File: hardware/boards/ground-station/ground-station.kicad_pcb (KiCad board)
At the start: 4 copper layers, 65 x 56.5 mm, 118 parts, among them J1 USB_A, J101 Raspberry_Pi_2_3, J102 Conn_01x15, J2 Barrel_Jack, J201 U.FL, J202 U.FL, J203 U.FL, J3 Conn_Coaxial, U201 SX1262IMLTRT, U202 RX5808, U203 SW-GPS01, U204 SKY13453-385LF, U3 TPS564242DRLR, U601 ADV7282A-M, U602 AP2127K-1.8, U603 AP2127K-1.8, Y201 32 MHz, Y601 28.63636 MHz

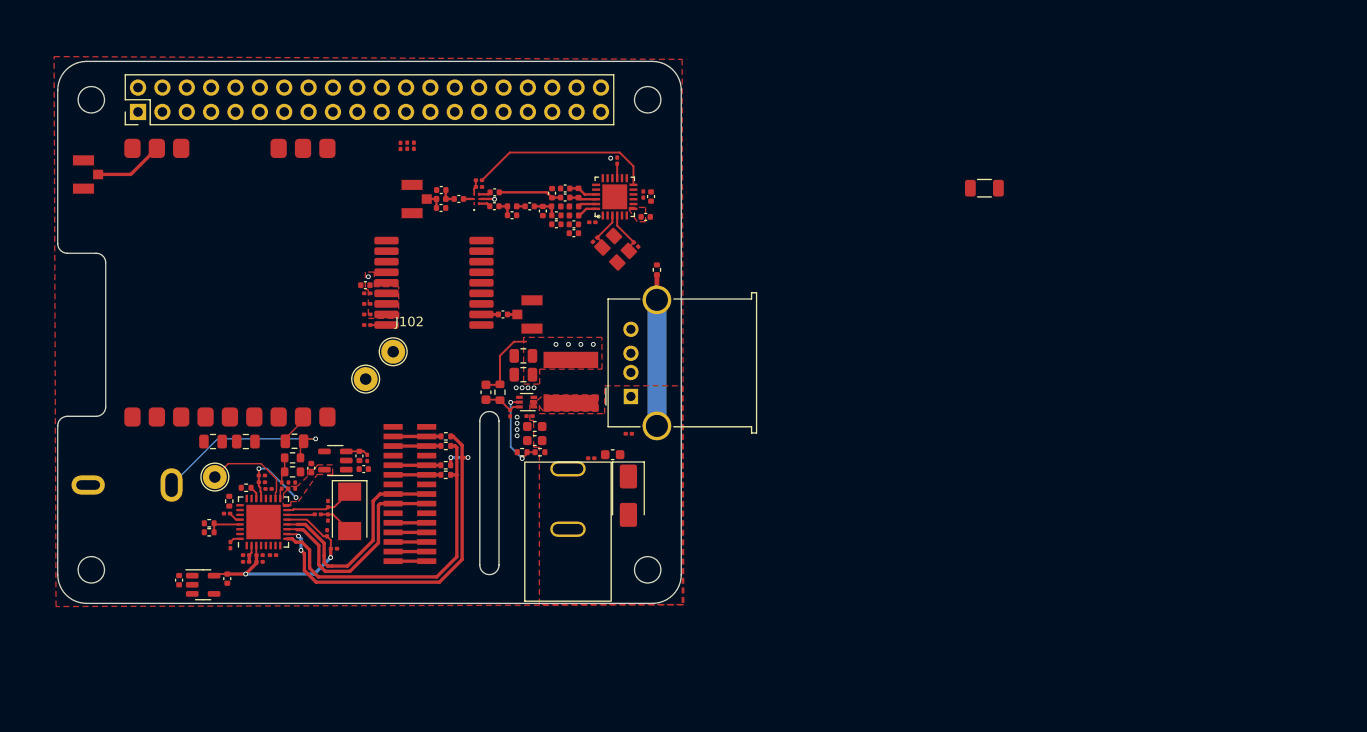
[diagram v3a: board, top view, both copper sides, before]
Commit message: Finished initial layout
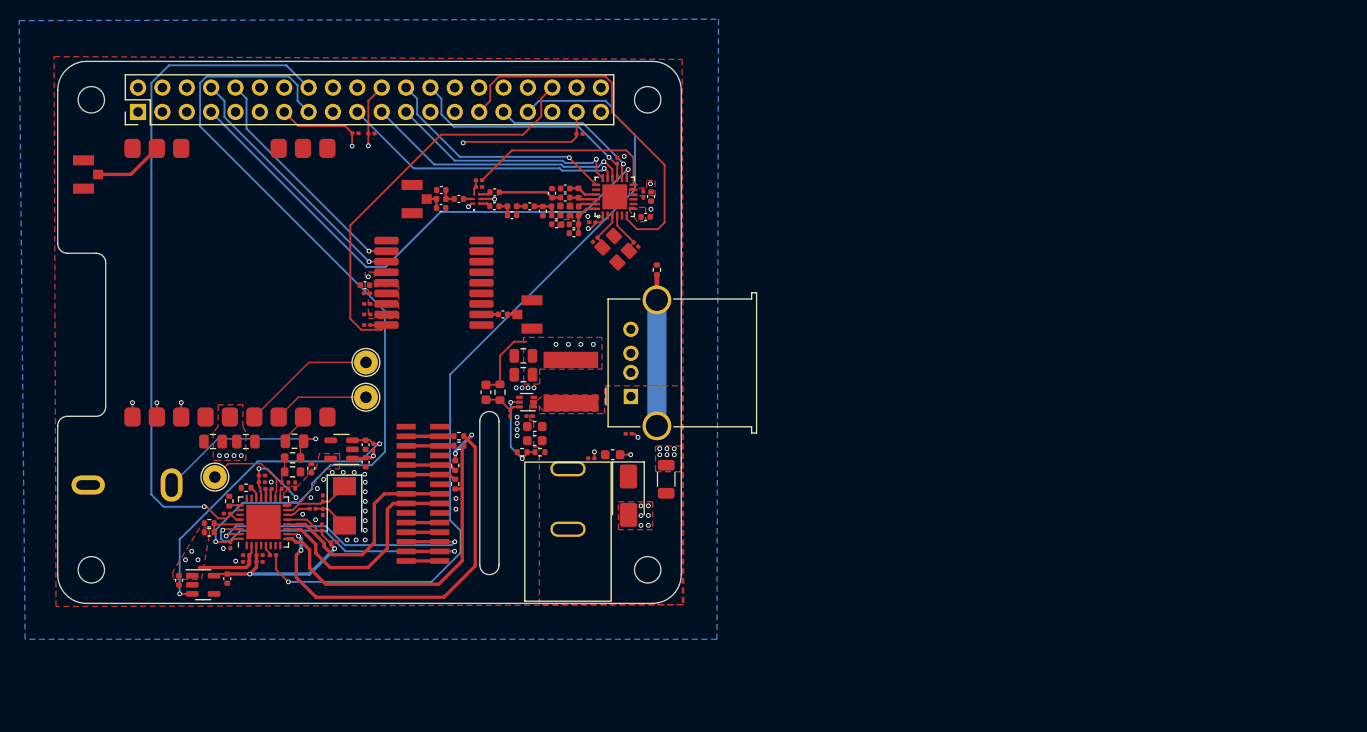
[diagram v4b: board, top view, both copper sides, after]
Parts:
- moved R3 45.0 mm to (163.6, 109.4), turned to 90 degrees
- moved R203 18.0 mm to (154.6, 73.4), turned to 0 degrees
- moved R204 4.88 mm to (131.2, 73.4), turned to 0 degrees
- moved R202 4.61 mm to (132.9, 73.4), turned to 0 degrees
- moved TP1 3.05 mm to (132.3, 97.3)
- moved TP2 1.89 mm to (132.3, 100.9)
- moved R24 1.37 mm to (141.6, 109.9), turned to 90 degrees
- moved J102 1.36 mm to (138.3, 111.0)
- moved R25 1.36 mm to (142.0, 105.0)
- moved R26 1.36 mm to (142.0, 106.0)
- moved C610 1.33 mm to (132.3, 105.8)
- moved R606 1.33 mm to (133.1, 106.1)
- moved U603 1.33 mm to (129.8, 106.3)
- moved R23 0.98 mm to (141.6, 108.0), turned to -90 degrees
- moved C603 0.79 mm to (127.8, 112.8)
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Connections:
- J201 pad 2: unconnected-(J201-Ext-Pad2) -> GND
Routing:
- net /~{DIGITIZER_INTRQ}: track 0.00 -> 87.9 mm, vias 0 -> 1
- net /~{DIGITIZER_PWRDWN}: track 1.14 -> 85.8 mm, vias 0 -> 1
- net /~{DIGITIZER_RESET}: track 1.30 -> 71.9 mm, vias 0 -> 1
- net /VIDEO_CH2: track 0.00 -> 60.4 mm, vias 0 -> 2
- net /DIGITAL_RADIO_DIO1: track 0.00 -> 55.3 mm, vias 0 -> 1
- net +5V: track 0.00 -> 52.8 mm, vias 0 -> 4
- net /VIDEO_CH1: track 0.00 -> 49.4 mm, vias 0 -> 2
- net /VIDEO_CH3: track 0.00 -> 45.0 mm, vias 0 -> 2
- net /~{GPS_RESET}: track 1.68 -> 44.0 mm
- net /DIGITAL_RADIO_DIO3: track 0.00 -> 38.5 mm
- net /Video Digitizer/VID_EN_1V8: track 2.34 -> 35.0 mm, vias 0 -> 2
- net /CAM_SDA: track 3.50 -> 33.7 mm, vias 0 -> 2
- net /DIGITAL_RADIO_MOSI: track 0.00 -> 29.5 mm, vias 0 -> 1
- net /CAM_SCL: track 3.50 -> 31.8 mm, vias 0 -> 2
- net /DIGITAL_RADIO_MISO: track 0.00 -> 27.9 mm, vias 0 -> 1
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- added copper zone on In2.Cu, net +3V3
- added copper zone on In2.Cu, net +5V
- added copper zone on B.Cu, net GND
- added copper zone on F.Cu, net Net-(C219-Pad1)
- added copper zone on F.Cu, net Net-(J101-5V-Pad2)
- added copper zone on In2.Cu, net Net-(J101-5V-Pad2)

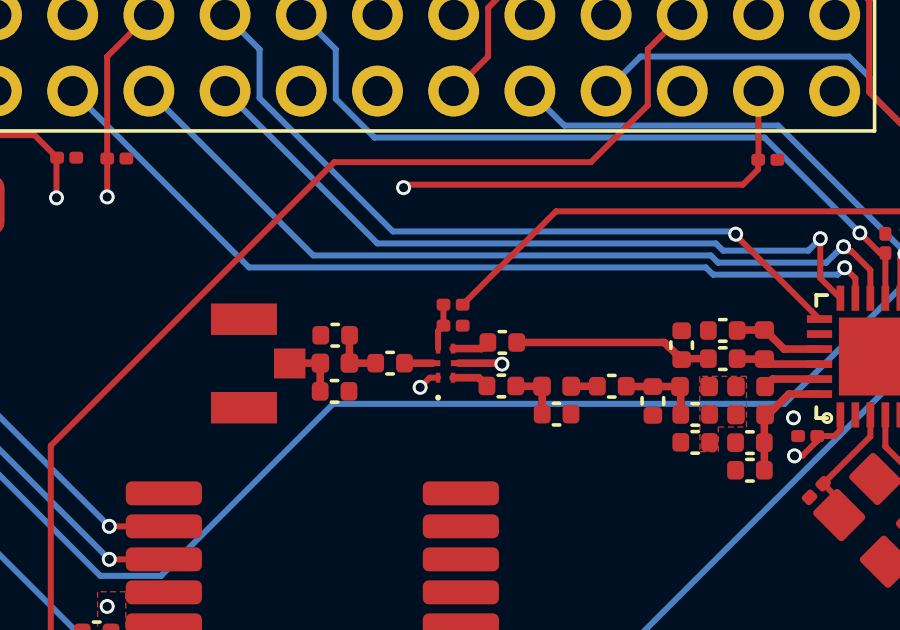
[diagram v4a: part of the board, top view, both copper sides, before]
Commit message: Added voltage divider to RF switch VTCL pin to keep voltage to 1.8V. Adjusted cap size to keep RC cutoff frequency consistent
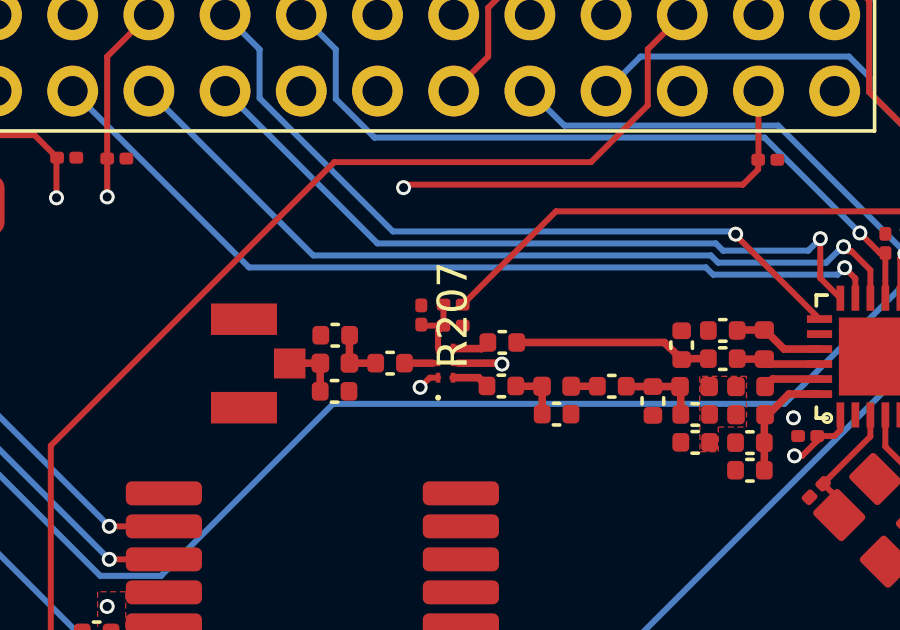
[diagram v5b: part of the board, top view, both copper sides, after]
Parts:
- added R207: 2.7k, Resistor_SMD:R_0201_0603Metric, F.Cu at (143.0, 78.6)
- C226: value 1n -> 100p
- R206: value 100R -> 2.2k
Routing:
- net Net-(U204-VTCL): track 1.54 -> 2.29 mm
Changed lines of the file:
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@@
         (effects (font (size 1 1) (thickness 0.15)))
     )
-    (fp_text value "1n" (at 0 1.05) (layer "F.Fab")
+    (fp_text value "100p" (at 0 1.05) (layer "F.Fab")
         (effects (font (size 1 1) (thickness 0.15)))
     )
@@
         (effects (font (size 1 1) (thickness 0.15)))
     )
-    (fp_text value "100R" (at 0 1.05) (layer "F.Fab")
+    (fp_text value "2.2k" (at 0 1.05) (layer "F.Fab")
         (effects (font (size 1 1) (thickness 0.15)))
     )
@@
   )
   (footprint "Resistor_SMD:R_0201_0603Metric" (layer "F.Cu")
+    (at 143.04 78.615 -90)
+    (descr "Resistor SMD 0201 (0603 Metric), square (rectangular) end terminal, IPC_7351 nominal, (Body size source: https://www.vishay.com/docs/20052/crcw0201e3.pdf), generated with kicad-footprint-generator")
+    (tags "resistor")
+    (property "Sheetfile" "radio.kicad_sch")
+    (property "Sheetname" "Radios")
+    (property "ki_description" "Resistor")
+    (property "ki_keywords" "R res resistor")
+    (attr smd)
+    (fp_text reference "R207" (at 0 -1.05 90) (layer "F.SilkS")
+        (effects (font (size 1 1) (thickness 0.15)))
+    )
+    (fp_text value "2.7k" (at 0 1.05 90) (layer "F.Fab")
+        (effects (font (size 1 1) (thickness 0.15)))
+    )
+    (fp_text user "${REFERENCE}" (at 0 -0.68 90) (layer "F.Fab")
+        (effects (font (size 0.25 0.25) (thickness 0.04)))
+    )
+    (fp_line (start -0.7 -0.35) (end 0.7 -0.35)
+      (stroke (width 0.05) (type solid)) (layer "F.CrtYd"))
+    (fp_line (start -0.7 0.35) (end -0.7 -0.35)
+      (stroke (width 0.05) (type solid)) (layer "F.CrtYd"))
+    (fp_line (start 0.7 -0.35) (end 0.7 0.35)
+      (stroke (width 0.05) (type solid)) (layer "F.CrtYd"))
+    (fp_line (start 0.7 0.35) (end -0.7 0.35)
+      (stroke (width 0.05) (type solid)) (layer "F.CrtYd"))
+    (fp_line (start -0.3 -0.15) (end 0.3 -0.15)
+      (stroke (width 0.1) (type solid)) (layer "F.Fab"))
+    (fp_line (start -0.3 0.15) (end -0.3 -0.15)
+      (stroke (width 0.1) (type solid)) (layer "F.Fab"))
+    (fp_line (start 0.3 -0.15) (end 0.3 0.15)
+      (stroke (width 0.1) (type solid)) (layer "F.Fab"))
+    (fp_line (start 0.3 0.15) (end -0.3 0.15)
+      (stroke (width 0.1) (type solid)) (layer "F.Fab"))
+    (pad "" smd roundrect (at -0.345 0 270) (size 0.318 0.36) (layers "F.Paste") (roundrect_rratio 0.25))
+    (pad "" smd roundrect (at 0.345 0 270) (size 0.318 0.36) (layers "F.Paste") (roundrect_rratio 0.25))
+    (pad "1" smd roundrect (at -0.32 0 270) (size 0.46 0.4) (layers "F.Cu" "F.Mask") (roundrect_rratio 0.25)
+      (net 3 "GND") (pintype "passive"))
+    (pad "2" smd roundrect (at 0.32 0 270) (size 0.46 0.4) (layers "F.Cu" "F.Mask") (roundrect_rratio 0.25)
+      (net 31 "Net-(U204-VTCL)") (pintype "passive"))
+    (model "${KICAD6_3DMODEL_DIR}/Resistor_SMD.3dshapes/R_0201_0603Metric.wrl"
+      (offset (xyz 0 0 0))
+      (scale (xyz 1 1 1))
+      (rotate (xyz 0 0 0))
+    )
+  )
+  (footprint "Resistor_SMD:R_0201_0603Metric" (layer "F.Cu")
     (at 132.89 73.4)
     (descr "Resistor SMD 0201 (0603 Metric), square (rectangular) end terminal, IPC_7351 nominal, (Body size source: https://www.vishay.com/docs/20052/crcw0201e3.pdf), generated with kicad-footprint-generator")
@@
   (segment (start 145.055 79.735) (end 145.26 79.53) (width 0.254) (layer "F.Cu") (net 30))
   (segment (start 143.6 79.735) (end 143.6 79.15) (width 0.2) (layer "F.Cu") (net 31))
+  (segment (start 143.075 78.97) (end 143.04 78.935) (width 0.2) (layer "F.Cu") (net 31))
   (segment (start 143.6 79.15) (end 143.78 78.97) (width 0.2) (layer "F.Cu") (net 31))
+  (segment (start 143.78 78.97) (end 143.075 78.97) (width 0.2) (layer "F.Cu") (net 31))
   (segment (start 143.78 78.97) (end 143.78 78.27) (width 0.2) (layer "F.Cu") (net 31))
   (segment (start 140.645 79.295) (end 140.65 79.29) (width 0.254) (layer "F.Cu") (net 33))

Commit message: base station layout review
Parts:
- added C231: 100n, Capacitor_SMD:C_0201_0603Metric, F.Cu at (155.9, 82.7)
- added R208: 0, Resistor_SMD:R_0402_1005Metric, F.Cu at (127.1, 105.5)
- moved R23 14.3 mm to (140.8, 122.2), turned to 90 degrees
- moved R24 13.9 mm to (142.7, 123.8), turned to -45 degrees
- moved R25 13.3 mm to (142.1, 118.2), turned to 90 degrees
- moved C227 12.7 mm to (143.3, 81.5)
- moved R26 10.6 mm to (143.3, 116.5), turned to 90 degrees
- turned J102 to 180 degrees
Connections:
- J3 pad 1: /Radios/VIDEO_OUT -> Net-(J3-In)
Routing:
- net /CAM_CK_N: track 22.4 -> 50.0 mm
- net /CAM_CK_P: track 23.3 -> 50.1 mm
- net Net-(J3-In): track 0.00 -> 17.6 mm, vias 0 -> 1
- net /Radios/VIDEO_OUT: track 20.2 -> 3.32 mm, vias 1 -> 0
- net /CAM_D1_CONN_P: track 5.38 -> 18.6 mm, vias 0 -> 2
- net /CAM_D1_CONN_N: track 5.34 -> 15.3 mm, vias 0 -> 2
- net /CAM_SDA: track 33.7 -> 39.5 mm
- net /CAM_D0_P: track 35.4 -> 41.1 mm
- net /CAM_D0_N: track 44.9 -> 39.9 mm, vias 4 -> 0
- net unconnected-(J102-Pin_15-Pad15): track 3.50 -> 0.00 mm
- net /CAM_SCL: track 31.8 -> 35.2 mm
- net /CAM_D0_CONN_P: track 4.99 -> 7.18 mm
- net /CAM_D0_CONN_N: track 4.99 -> 6.66 mm
- net /~{DIGITIZER_INTRQ}: track 87.9 -> 86.5 mm
- net +5V: track 52.8 -> 54.0 mm
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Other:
- board size 65 x 56.5 mm -> 65 x 59.5 mm

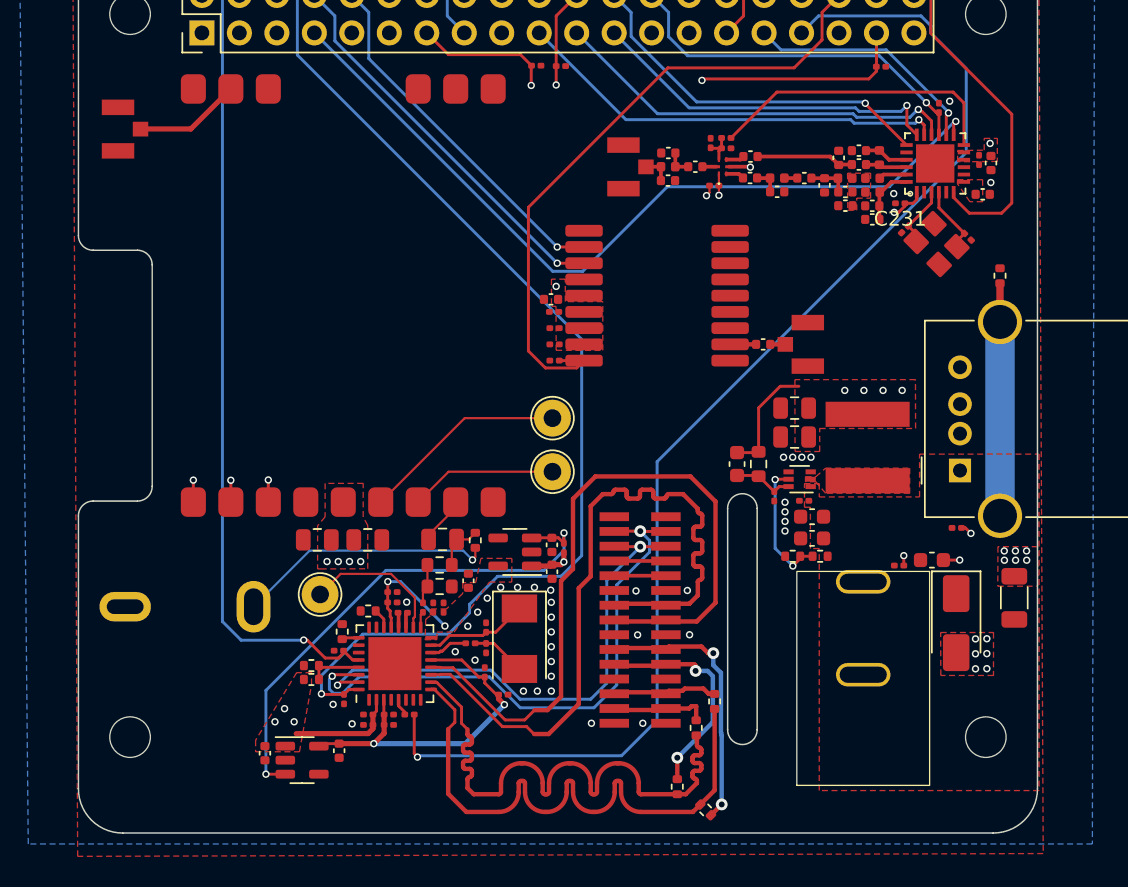
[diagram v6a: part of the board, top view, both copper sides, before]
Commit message: Added silkscreen
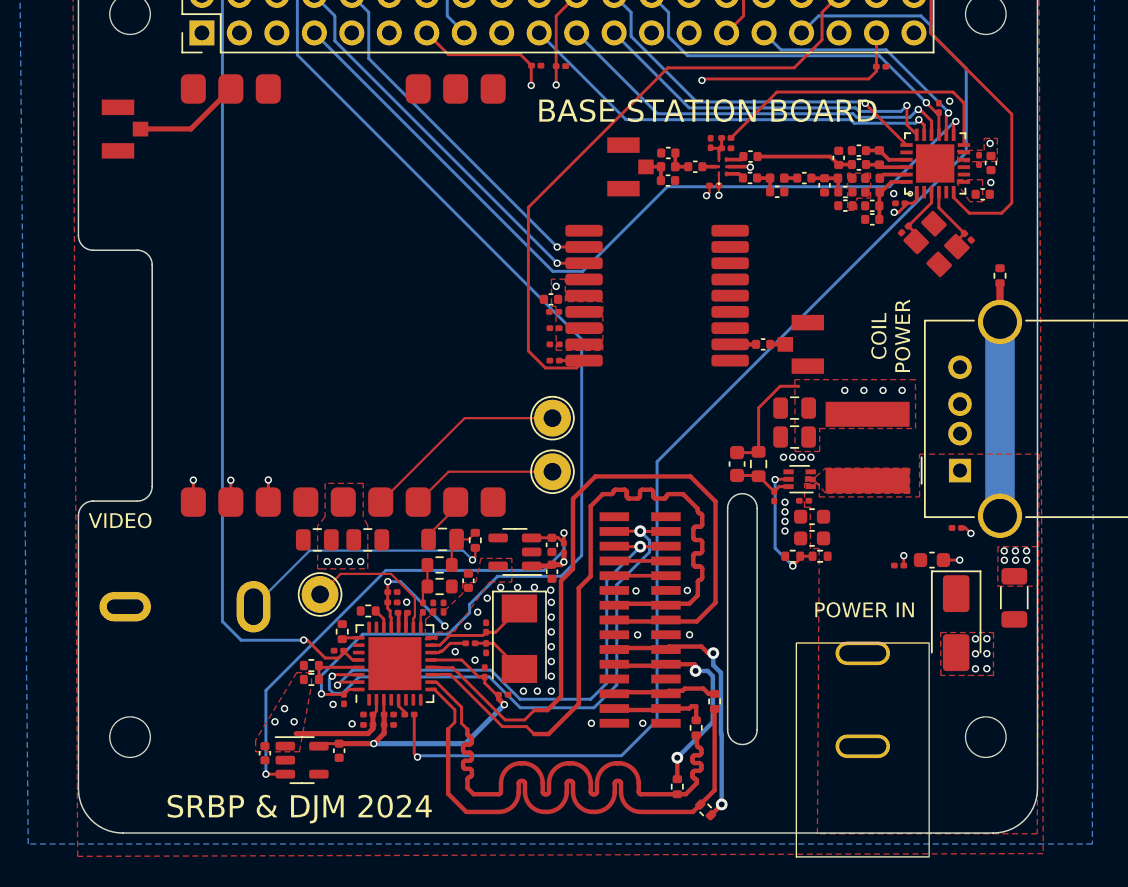
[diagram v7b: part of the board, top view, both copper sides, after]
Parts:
- added G***: LOGO, LOGO, B.Cu at (118.6, 91.6)
- moved J2 4.85 mm to (153.3, 119.5)
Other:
- board text added: "BASE STATION BOARD"
- board text added: "COIL POWER"
- board text added: "POWER IN"
- board text added: "SRBP & DJM 2024"
- board text added: "VIDEO"
